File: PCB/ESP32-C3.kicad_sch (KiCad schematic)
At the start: 32 parts, among them J1 HCZZ0039-3, J2 DPS_PPS_Right_Angle, SW2 TS4535TP 250gf 009, U1 USB-C-16P-SMD, U3 ESP32-C3, Y1 40MHz_S3240000151040

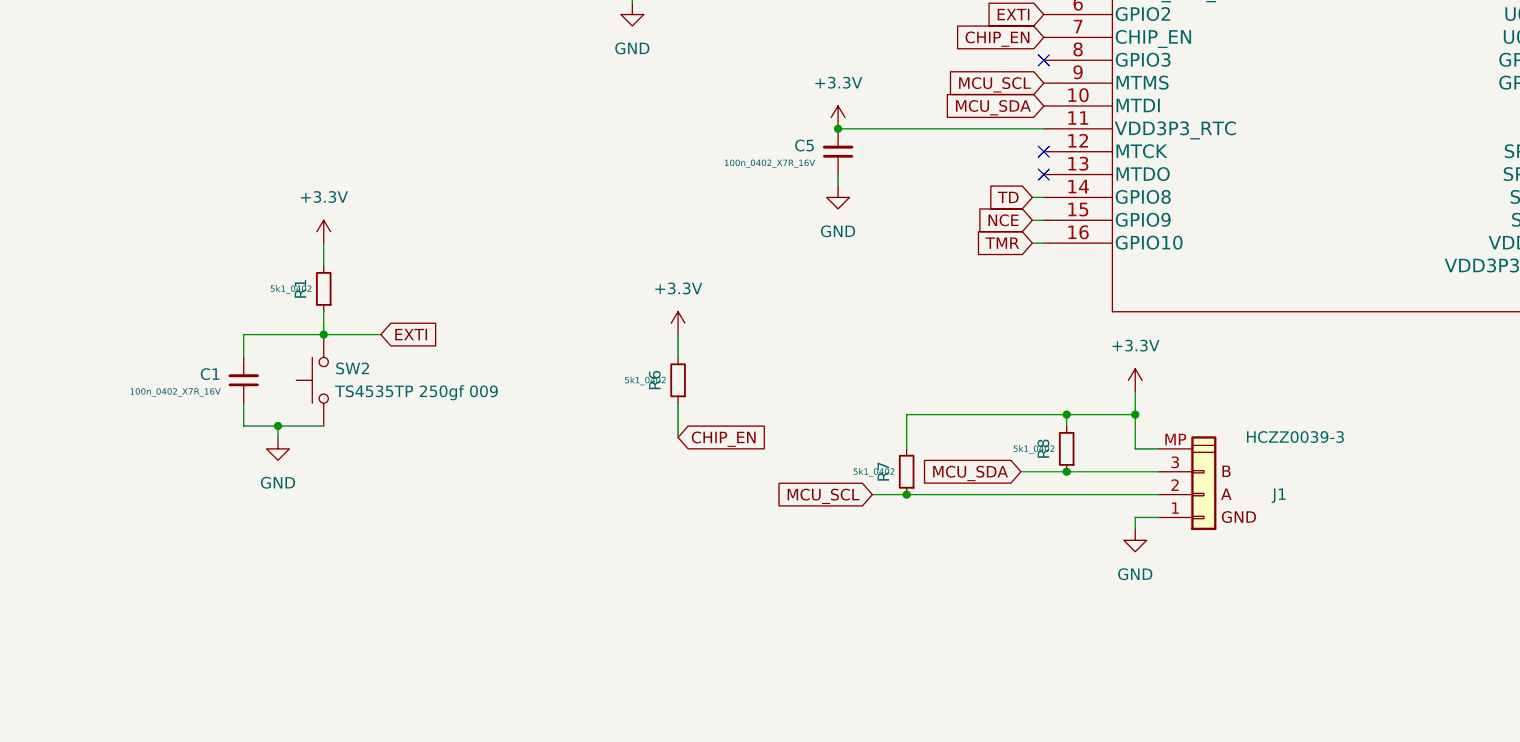
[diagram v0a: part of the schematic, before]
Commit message: Boot Button hinzugefügt
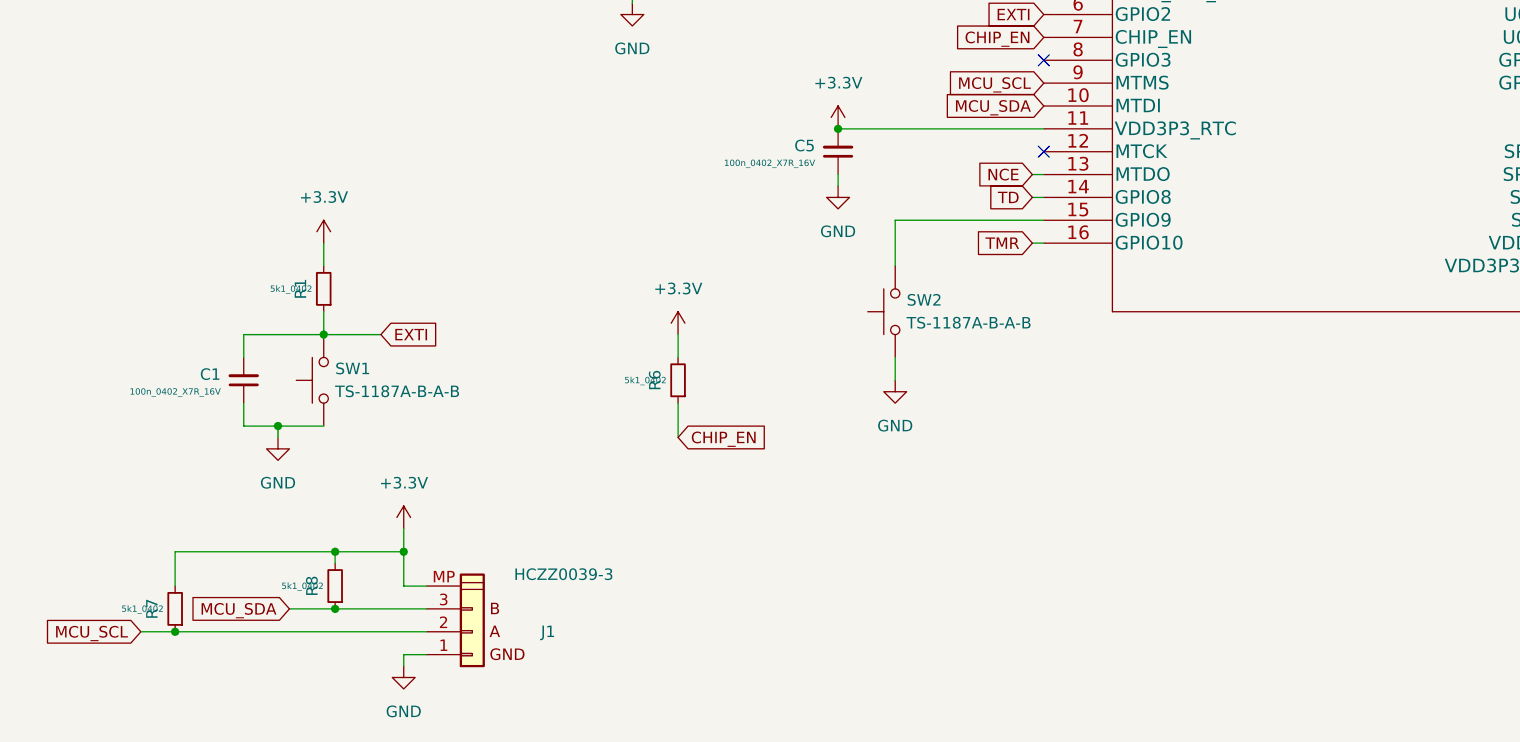
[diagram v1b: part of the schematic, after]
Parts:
- removed SW2: TS4535TP 250gf 009, switch:SW_SPST_TL3305B, symbol 1_switch:TS4535TP 250gf 009
- added SW1, SW2: TS-1187A-B-A-B, switch:SW_SPST_TL3305B, symbol 1_switch:TS-1187A-B-A-B
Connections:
- net EXTI: now also SW1.2
- net GND: now also SW1.1, SW2.1
- net NCE: now also U3.13 (MTDO); no longer U3.15 (GPIO9)
- new net: SW2.2, U3.15 (GPIO9)
- no-connect marks 17 -> 16
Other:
- moved on the sheet: J1, R7, R8

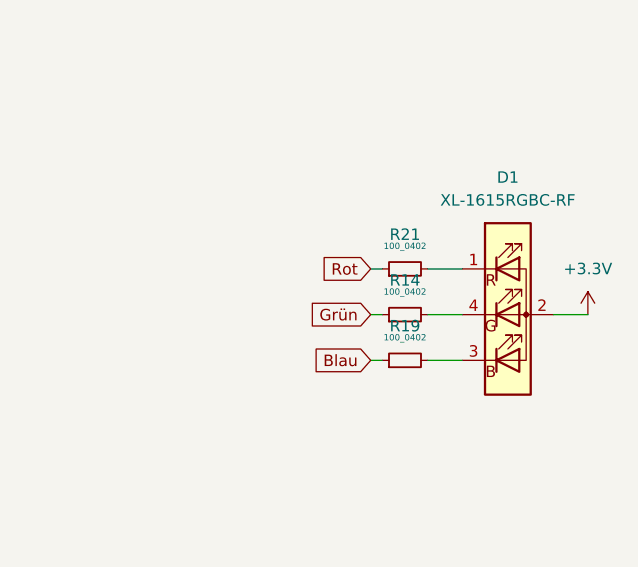
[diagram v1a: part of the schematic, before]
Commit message: LDO hinzugefügt
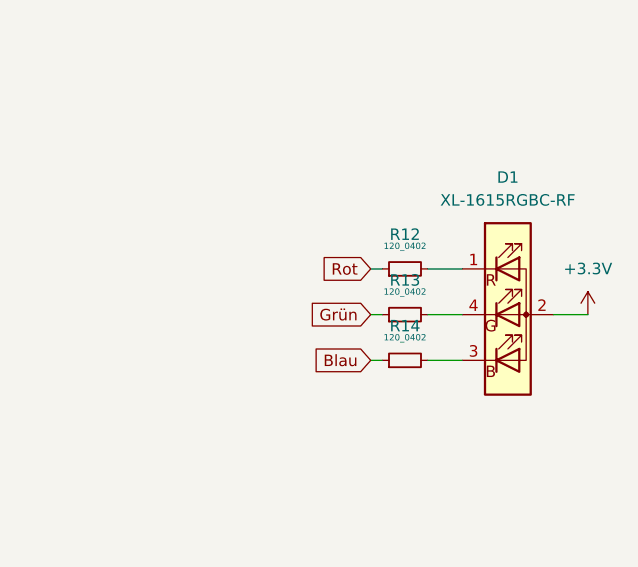
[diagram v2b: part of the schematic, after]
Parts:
- removed R14, R19, R21: 100_0402, Resistor_SMD:R_0402_1005Metric, symbol resistor_smd_standard:100_0402
- added R12, R13, R14: 120_0402, Resistor_SMD:R_0402_1005Metric, symbol resistor_smd_standard:120_0402
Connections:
- net Blau: now also R14.1
- net Grün: now also R13.1
- net Rot: now also R12.1
- net at D1.3 (BK): now also R14.2
- net at D1.1 (RK): now also R12.2
- net at D1.4 (GK): now also R13.2

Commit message: Kleine Verbesserungen
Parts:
- D1: footprint LEDSMD:LED_0606_1432 -> LEDSMD:LED_0606_1432_correct
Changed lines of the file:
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@@
 			)
 		)
-		(property "Footprint" "LEDSMD:LED_0606_1432"
+		(property "Footprint" "LEDSMD:LED_0606_1432_correct"
 			(at 255.27 34.29 0)
 			(effects
